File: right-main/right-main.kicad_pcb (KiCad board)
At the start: 2 copper layers, 150.4 x 123.8 mm, 209 parts, among them J1 USBCONN, P1 CONN_4, P2 CONN_5, P3 CONN_6, SW1 PTS525SM10, SW11 SPST, SW12 SPST, SW13 SPST, SW14 SPST, SW15 SPST, SW16 SPST, SW17 SPST, SW21 SPST, SW22 SPST, SW23 SPST, SW24 SPST, SW25 SPST, SW26 SPST, SW27 SPST, SW31 SPST, SW32 SPST, SW33 SPST, SW34 SPST, SW35 SPST, SW36 SPST, SW37 SPST, SW41 SPST, SW42 SPST, SW43 SPST, SW44 SPST, SW45 SPST, SW46 SPST, SW47 SPST, SW52 SPST, SW53 SPST, SW54 SPST, SW55 SPST, SW56 SPST, SW57 SPST, U1 ATMEGA32U4, U2 CAT24C256, X1 16Mhz

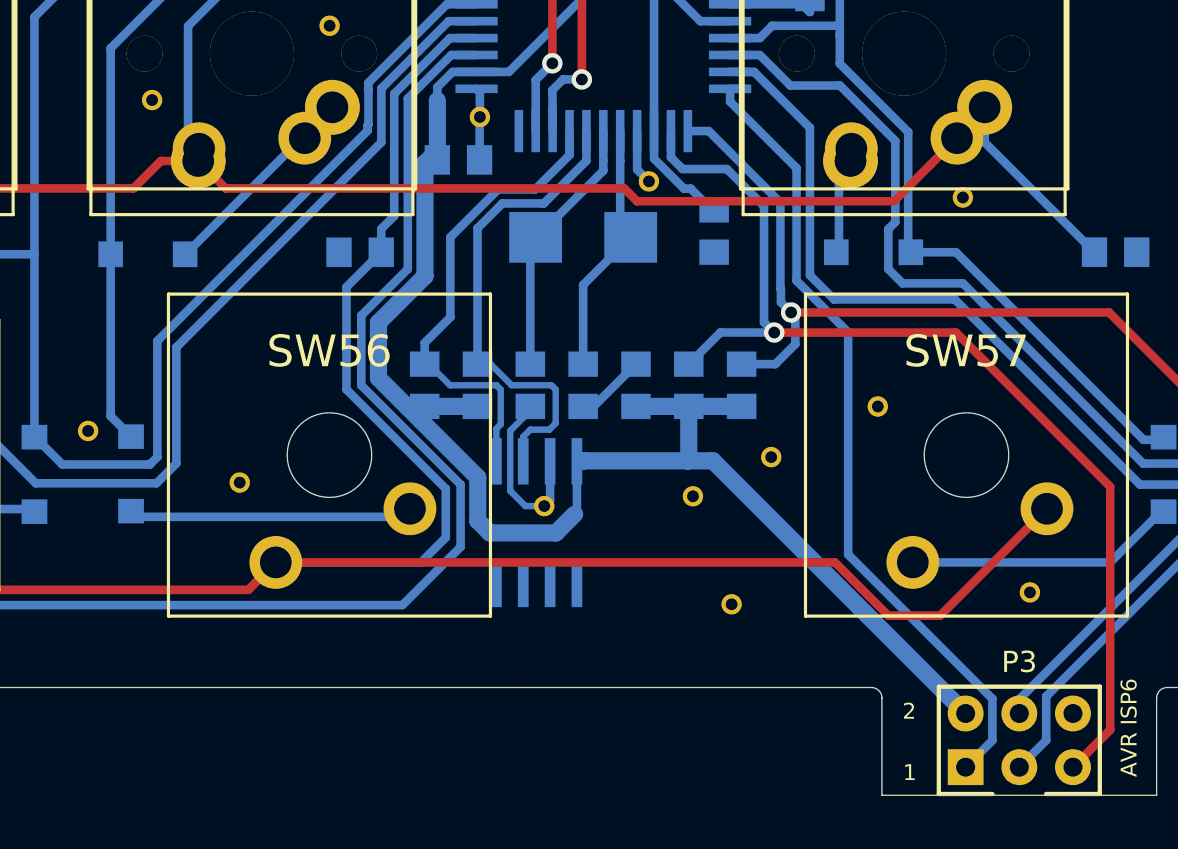
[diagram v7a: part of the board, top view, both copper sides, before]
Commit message: switch 56 right
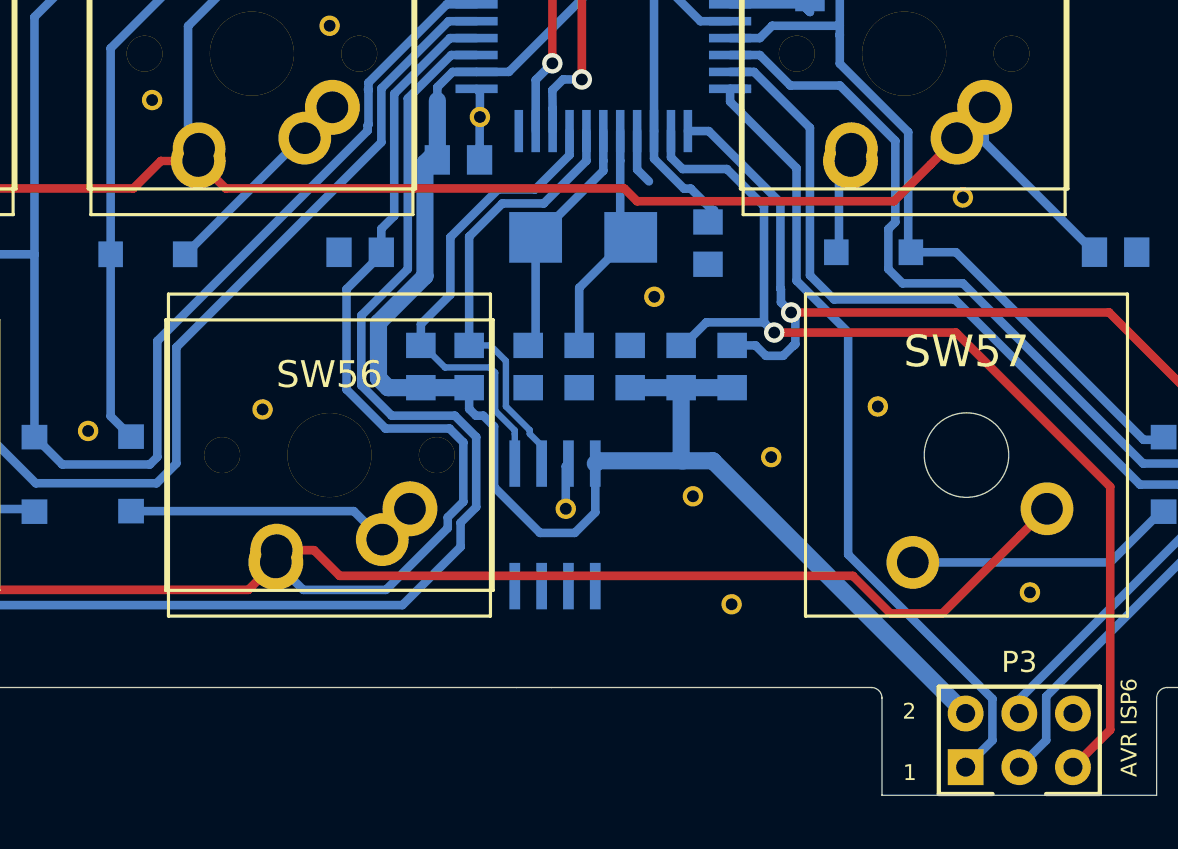
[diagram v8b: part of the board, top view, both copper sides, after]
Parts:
- added via 38/22mil: VAL**, ugl:via_38_22mil, F.Cu at (225.4, 132.2)
- SW56: footprint UGL:Cherry_MX -> ugl:Cherry-MX-Matias-Hybrid
- moved via 38/22mil 3.62 mm to (206.9, 137.5)
- moved via 38/22mil 1.02 mm to (221.2, 142.2)
- moved R4 0.99 mm to (229.1, 135.5)
- moved R23 0.97 mm to (216.7, 135.5)
- moved R1 0.96 mm to (226.7, 135.5)
- moved C6 0.93 mm to (224.3, 135.5)
- moved C2 0.91 mm to (221.9, 135.5)
- moved R24 0.91 mm to (214.4, 135.5)
- moved C1 0.89 mm to (219.5, 135.5)
- moved U2 0.88 mm to (220.7, 143.0)
- moved C15 0.64 mm to (228.0, 129.7)
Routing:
- net GND: track 67.2 -> 57.5 mm
- net /ROW5: track 168.3 -> 171.8 mm
- net VCC: track 438.8 -> 436.1 mm
- net /RX2: track 145.5 -> 147.9 mm
- net Net-(D56-Pad2): track 13.5 -> 15.6 mm
- net /SCL: track 23.1 -> 21.3 mm
- net /XTAL2: track 14.8 -> 14.3 mm
